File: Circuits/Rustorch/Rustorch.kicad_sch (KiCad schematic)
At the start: 57 parts, among them CN1 USB_C_Receptacle_USB2.0_16P, CN2 OLED_128x64_IIC, Q1 2SC1815, Q2 2SC1815, Q3 2SC1815, Q4 2SC1815, SW1 SW_POWER (5P), SW2 RESET, SW3 SW_BOOT, SW4 SW_UP, SW5 SW_LEFT, SW6 SW_RIGHT, SW7 SW_DOWN, SW8 SW_A, SW9 SW_B, U1 ESP32-C6-WROOM-1, U2 BA033CC0T, U3 OSL10561-L*, U4 OSL10561-L*, U5 OSL10561-L*, U6 OSL10561-L*

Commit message: (Rustorch) 回路図フットプリント割り当て (可変抵抗は未)
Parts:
- CN1: footprint (none) -> Connector_USB:USB_C_Receptacle_XKB_U262-16XN-4BVC11
- CN2: footprint (none) -> extsui:OLED_128x64_0.96inch
- D1, D3, D4, D5, D6, D7, D8: footprint (none) -> Diode_THT:D_DO-35_SOD27_P5.08mm_Vertical_AnodeUp
- D2: footprint (none) -> LED_THT:LED_D3.0mm
- R1, R10, R11, R12, R13, R14, R15, R16, R17, R18, R19, R2, R4, R5, R6, R7, R8, R9: footprint (none) -> Resistor_THT:R_Axial_DIN0207_L6.3mm_D2.5mm_P7.62mm_Horizontal
- R20, R21, R22, R23, R3: footprint (none) -> Resistor_THT:R_Axial_DIN0207_L6.3mm_D2.5mm_P2.54mm_Vertical
- SW1: footprint (none) -> Button_Switch_THT:SW_Slide_SPDT_Straight_CK_OS102011MS2Q
- SW2, SW3, SW4, SW5, SW6, SW7, SW8, SW9: footprint (none) -> Button_Switch_THT:SW_PUSH_6mm_H7.3mm
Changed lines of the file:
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@@
 			)
 		)
-		(property "Footprint" ""
+		(property "Footprint" "Resistor_THT:R_Axial_DIN0207_L6.3mm_D2.5mm_P7.62mm_Horizontal"
 			(at 262.89 91.44 0)
 			(effects
@@
 			)
 		)
-		(property "Footprint" ""
+		(property "Footprint" "Resistor_THT:R_Axial_DIN0207_L6.3mm_D2.5mm_P7.62mm_Horizontal"
 			(at 59.69 54.61 0)
 			(effects
@@
 			)
 		)
-		(property "Footprint" ""
+		(property "Footprint" "Button_Switch_THT:SW_Slide_SPDT_Straight_CK_OS102011MS2Q"
 			(at 215.9 48.26 0)
 			(effects
@@
 			)
 		)
-		(property "Footprint" ""
+		(property "Footprint" "LED_THT:LED_D3.0mm"
 			(at 226.06 59.69 90)
 			(effects
@@
 			)
 		)
-		(property "Footprint" ""
+		(property "Footprint" "Resistor_THT:R_Axial_DIN0207_L6.3mm_D2.5mm_P7.62mm_Horizontal"
 			(at 41.91 147.32 0)
 			(effects
@@
 			)
 		)
-		(property "Footprint" ""
+		(property "Footprint" "Resistor_THT:R_Axial_DIN0207_L6.3mm_D2.5mm_P7.62mm_Horizontal"
 			(at 48.26 144.78 0)
 			(effects
@@
 			)
 		)
-		(property "Footprint" ""
+		(property "Footprint" "Resistor_THT:R_Axial_DIN0207_L6.3mm_D2.5mm_P7.62mm_Horizontal"
 			(at 113.03 72.39 0)
 			(effects
@@
 			)
 		)
-		(property "Footprint" ""
+		(property "Footprint" "Resistor_THT:R_Axial_DIN0207_L6.3mm_D2.5mm_P2.54mm_Vertical"
 			(at 49.53 172.72 0)
 			(effects
@@
 			)
 		)
-		(property "Footprint" ""
+		(property "Footprint" "Button_Switch_THT:SW_PUSH_6mm_H7.3mm"
 			(at 245.11 124.46 0)
 			(effects
@@
 			)
 		)
-		(property "Footprint" ""
+		(property "Footprint" "Resistor_THT:R_Axial_DIN0207_L6.3mm_D2.5mm_P7.62mm_Horizontal"
 			(at 93.98 55.88 0)
 			(effects
@@
 			)
 		)
-		(property "Footprint" ""
+		(property "Footprint" "Diode_THT:D_DO-35_SOD27_P5.08mm_Vertical_AnodeUp"
 			(at 250.19 153.67 90)
 			(effects
@@
 			)
 		)
-		(property "Footprint" ""
+		(property "Footprint" "Resistor_THT:R_Axial_DIN0207_L6.3mm_D2.5mm_P7.62mm_Horizontal"
 			(at 232.41 109.22 0)
 			(effects
@@
 			)
 		)
-		(property "Footprint" ""
+		(property "Footprint" "extsui:OLED_128x64_0.96inch"
 			(at 176.53 128.27 0)
 			(effects
@@
 			)
 		)
-		(property "Footprint" ""
+		(property "Footprint" "Diode_THT:D_DO-35_SOD27_P5.08mm_Vertical_AnodeUp"
 			(at 250.19 110.49 90)
 			(effects
@@
 			)
 		)
-		(property "Footprint" ""
+		(property "Footprint" "Diode_THT:D_DO-35_SOD27_P5.08mm_Vertical_AnodeUp"
 			(at 250.19 132.08 90)
 			(effects
@@
 			)
 		)
-		(property "Footprint" ""
+		(property "Footprint" "Button_Switch_THT:SW_PUSH_6mm_H7.3mm"
 			(at 227.33 118.11 0)
 			(effects
@@
 			)
 		)
-		(property "Footprint" ""
+		(property "Footprint" "Resistor_THT:R_Axial_DIN0207_L6.3mm_D2.5mm_P7.62mm_Horizontal"
 			(at 245.11 91.44 0)
 			(effects
@@
 			)
 		)
-		(property "Footprint" ""
+		(property "Footprint" "Button_Switch_THT:SW_PUSH_6mm_H7.3mm"
 			(at 245.11 146.05 0)
 			(effects
@@
 			)
 		)
-		(property "Footprint" ""
+		(property "Footprint" "Resistor_THT:R_Axial_DIN0207_L6.3mm_D2.5mm_P7.62mm_Horizontal"
 			(at 41.91 132.08 0)
 			(effects
@@
 			)
 		)
-		(property "Footprint" ""
+		(property "Footprint" "Resistor_THT:R_Axial_DIN0207_L6.3mm_D2.5mm_P7.62mm_Horizontal"
 			(at 48.26 139.7 0)
 			(effects
@@
 			)
 		)
-		(property "Footprint" ""
+		(property "Footprint" "Diode_THT:D_DO-35_SOD27_P5.08mm_Vertical_AnodeUp"
 			(at 267.97 132.08 90)
 			(effects
@@
 			)
 		)
-		(property "Footprint" ""
+		(property "Footprint" "Button_Switch_THT:SW_PUSH_6mm_H7.3mm"
 			(at 262.89 102.87 0)
 			(effects
@@
 			)
 		)
-		(property "Footprint" ""
+		(property "Footprint" "Button_Switch_THT:SW_PUSH_6mm_H7.3mm"
 			(at 101.6 31.75 0)
 			(effects
@@
 			)
 		)
-		(property "Footprint" ""
+		(property "Footprint" "Resistor_THT:R_Axial_DIN0207_L6.3mm_D2.5mm_P7.62mm_Horizontal"
 			(at 232.41 152.4 0)
 			(effects
@@
 			)
 		)
-		(property "Footprint" ""
+		(property "Footprint" "Resistor_THT:R_Axial_DIN0207_L6.3mm_D2.5mm_P7.62mm_Horizontal"
 			(at 41.91 142.24 0)
 			(effects
@@
 			)
 		)
-		(property "Footprint" ""
+		(property "Footprint" "Diode_THT:D_DO-35_SOD27_P5.08mm_Vertical_AnodeUp"
 			(at 243.84 39.37 90)
 			(effects
@@
 			)
 		)
-		(property "Footprint" ""
+		(property "Footprint" "Diode_THT:D_DO-35_SOD27_P5.08mm_Vertical_AnodeUp"
 			(at 267.97 110.49 90)
 			(effects
@@
 			)
 		)
-		(property "Footprint" ""
+		(property "Footprint" "Resistor_THT:R_Axial_DIN0207_L6.3mm_D2.5mm_P7.62mm_Horizontal"
 			(at 48.26 134.62 0)
 			(effects
@@
 			)
 		)
-		(property "Footprint" ""
+		(property "Footprint" "Resistor_THT:R_Axial_DIN0207_L6.3mm_D2.5mm_P2.54mm_Vertical"
 			(at 41.91 170.18 0)
 			(effects
@@
 			)
 		)
-		(property "Footprint" ""
+		(property "Footprint" "Resistor_THT:R_Axial_DIN0207_L6.3mm_D2.5mm_P7.62mm_Horizontal"
 			(at 91.44 55.88 0)
 			(effects
@@
 			)
 		)
-		(property "Footprint" ""
+		(property "Footprint" "Resistor_THT:R_Axial_DIN0207_L6.3mm_D2.5mm_P7.62mm_Horizontal"
 			(at 41.91 137.16 0)
 			(effects
@@
 			)
 		)
-		(property "Footprint" ""
+		(property "Footprint" "Button_Switch_THT:SW_PUSH_6mm_H7.3mm"
 			(at 262.89 146.05 0)
 			(effects
@@
 			)
 		)
-		(property "Footprint" ""
+		(property "Footprint" "Resistor_THT:R_Axial_DIN0207_L6.3mm_D2.5mm_P2.54mm_Vertical"
 			(at 226.06 53.34 0)
 			(effects
@@
 			)
 		)
-		(property "Footprint" ""
+		(property "Footprint" "Resistor_THT:R_Axial_DIN0207_L6.3mm_D2.5mm_P2.54mm_Vertical"
 			(at 41.91 175.26 0)
 			(effects
@@
 			)
 		)
-		(property "Footprint" ""
+		(property "Footprint" "Button_Switch_THT:SW_PUSH_6mm_H7.3mm"
 			(at 245.11 102.87 0)
 			(effects
@@
 			)
 		)
-		(property "Footprint" ""
+		(property "Footprint" "Connector_USB:USB_C_Receptacle_XKB_U262-16XN-4BVC11"
 			(at 39.37 62.23 0)
 			(effects
@@
 			)
 		)
-		(property "Footprint" ""
+		(property "Footprint" "Resistor_THT:R_Axial_DIN0207_L6.3mm_D2.5mm_P2.54mm_Vertical"
 			(at 49.53 177.8 0)
 			(effects
@@
 			)
 		)
-		(property "Footprint" ""
+		(property "Footprint" "Diode_THT:D_DO-35_SOD27_P5.08mm_Vertical_AnodeUp"
 			(at 267.97 153.67 90)
 			(effects
@@
 			)
 		)
-		(property "Footprint" ""
+		(property "Footprint" "Resistor_THT:R_Axial_DIN0207_L6.3mm_D2.5mm_P7.62mm_Horizontal"
 			(at 110.49 33.02 0)
 			(effects
@@
 			)
 		)
-		(property "Footprint" ""
+		(property "Footprint" "Button_Switch_THT:SW_PUSH_6mm_H7.3mm"
 			(at 262.89 124.46 0)
 			(effects
@@
 			)
 		)
-		(property "Footprint" ""
+		(property "Footprint" "Resistor_THT:R_Axial_DIN0207_L6.3mm_D2.5mm_P7.62mm_Horizontal"
 			(at 59.69 52.07 0)
 			(effects
@@
 			)
 		)
-		(property "Footprint" ""
+		(property "Footprint" "Resistor_THT:R_Axial_DIN0207_L6.3mm_D2.5mm_P7.62mm_Horizontal"
 			(at 48.26 149.86 0)
 			(effects

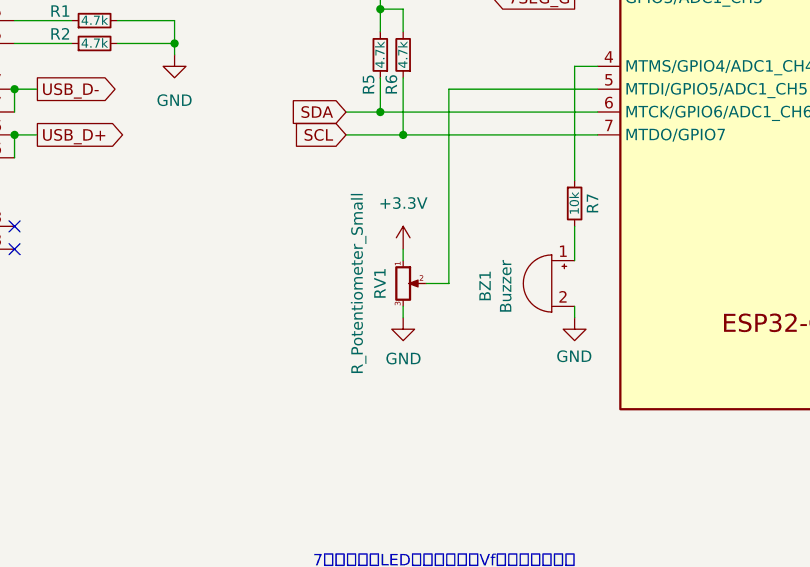
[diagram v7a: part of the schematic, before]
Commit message: (Rustorch) 可変抵抗 TSR-3386T のフットプリントを追加
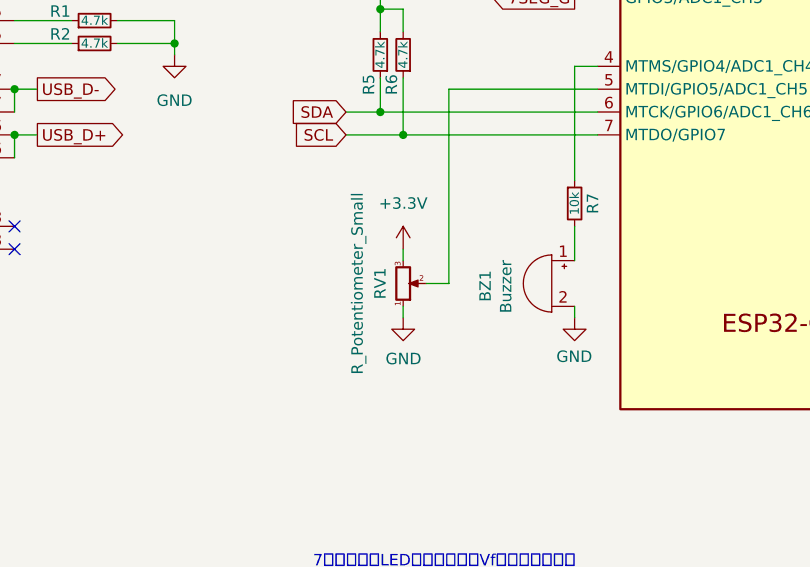
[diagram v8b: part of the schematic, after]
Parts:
- RV1: footprint (none) -> extsui:TSR_3386T
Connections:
- net +3.3V: now also RV1.3; no longer RV1.1
- net GND: now also RV1.1; no longer RV1.3
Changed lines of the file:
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@@
 		(lib_id "Device:R_Potentiometer_Small")
 		(at 93.98 81.28 0)
+		(mirror x)
 		(unit 1)
 		(exclude_from_sim no)
@@
 			)
 		)
-		(property "Footprint" ""
+		(property "Footprint" "extsui:TSR_3386T"
 			(at 93.98 81.28 0)
 			(effects
